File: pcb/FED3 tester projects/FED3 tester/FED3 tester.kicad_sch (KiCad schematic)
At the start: 27 parts, among them J1 USB4105-GF-A, U1 FT232RL, U2 LP5907MFX-3.3, U3 TPS79301-EP

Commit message: FED3 Tester - 1º routing finalizado
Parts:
- added L2: 40R@100MHz, Resistor_SMD:R_0805_2012Metric, symbol Device:R
- C1, C2, C3: footprint Capacitor_SMD:C_0402_1005Metric_Pad0.74x0.62mm_HandSolder -> Capacitor_SMD:C_0402_1005Metric
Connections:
- net USB+5V: now also L2.1
- new net RELAY+5V: L2.2
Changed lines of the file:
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@@
 	)
 	(junction
+		(at 81.28 36.83)
+		(diameter 0)
+		(color 0 0 0 0)
+	)
+	(junction
 		(at 147.32 88.9)
 		(diameter 0)
@@
 	(wire
 		(pts
+			(xy 81.28 36.83) (xy 85.09 36.83)
+		)
+		(stroke
+			(width 0)
+			(type default)
+		)
+	)
+	(wire
+		(pts
 			(xy 92.71 162.56) (xy 92.71 165.1)
 		)
@@
 	(wire
 		(pts
+			(xy 97.79 27.94) (xy 97.79 36.83)
+		)
+		(stroke
+			(width 0)
+			(type default)
+		)
+	)
+	(wire
+		(pts
 			(xy 74.93 41.91) (xy 71.12 41.91)
 		)
@@
 	(wire
 		(pts
+			(xy 92.71 36.83) (xy 97.79 36.83)
+		)
+		(stroke
+			(width 0)
+			(type default)
+		)
+	)
+	(wire
+		(pts
 			(xy 92.71 153.67) (xy 87.63 153.67)
 		)
@@
 	)
 	(symbol
+		(lib_id "power:+5V")
+		(at 97.79 27.94 0)
+		(mirror y)
+		(unit 1)
+		(exclude_from_sim no)
+		(in_bom yes)
+		(on_board yes)
+		(dnp no)
+		(property "Reference" "#PWR094"
+			(at 97.79 31.75 0)
+			(effects
+				(font
+					(size 1.27 1.27)
+				)
+				(hide yes)
+			)
+		)
+		(property "Value" "RELAY+5V"
+			(at 97.409 23.5458 0)
+			(effects
+				(font
+					(size 1.27 1.27)
+				)
+			)
+		)
+		(property "Footprint" ""
+			(at 97.79 27.94 0)
+			(effects
+				(font
+					(size 1.27 1.27)
+				)
+				(hide yes)
+			)
+		)
+		(property "Datasheet" ""
+			(at 97.79 27.94 0)
+			(effects
+				(font
+					(size 1.27 1.27)
+				)
+				(hide yes)
+			)
+		)
+		(property "Description" "Power symbol creates a global label with name \"+5V\""
+			(at 97.79 27.94 0)
+			(effects
+				(font
+					(size 1.27 1.27)
+				)
+				(hide yes)
+			)
+		)
+		(pin "1"
+		)
+		(instances
+			(project "FED3 tester"
+				(path "/2ba63f12-2fcd-4471-9636-2762cde37de8"
+					(reference "#PWR094")
+					(unit 1)
+				)
+			)
+		)
+	)
+	(symbol
 		(lib_id "power:GNDD")
 		(at 111.76 44.45 0)
@@
 			)
 		)
-		(property "Footprint" "Capacitor_SMD:C_0402_1005Metric_Pad0.74x0.62mm_HandSolder"
+		(property "Footprint" "Capacitor_SMD:C_0402_1005Metric"
 			(at 138.43 31.75 0)
 			(effects
@@
 	)
 	(symbol
+		(lib_id "Device:R")
+		(at 88.9 36.83 90)
+		(mirror x)
+		(unit 1)
+		(exclude_from_sim no)
+		(in_bom yes)
+		(on_board yes)
+		(dnp no)
+		(property "Reference" "L2"
+			(at 88.9 31.5722 90)
+			(effects
+				(font
+					(size 1.27 1.27)
+				)
+			)
+		)
+		(property "Value" "40R@100MHz"
+			(at 88.9 33.8836 90)
+			(effects
+				(font
+					(size 1.27 1.27)
+				)
+			)
+		)
+		(property "Footprint" "Resistor_SMD:R_0805_2012Metric"
+			(at 88.9 35.052 90)
+			(effects
+				(font
+					(size 1.27 1.27)
+				)
+				(hide yes)
+			)
+		)
+		(property "Datasheet" "~"
+			(at 88.9 36.83 0)
+			(effects
+				(font
+					(size 1.27 1.27)
+				)
+				(hide yes)
+			)
+		)
+		(property "Description" "FERRITE BEAD SMD 40Ω 2A 50mΩ"
+			(at 88.9 36.83 0)
+			(effects
+				(font
+					(size 1.27 1.27)
+				)
+				(hide yes)
+			)
+		)
+		(property "MPN" "MI0805K400R-10"
+			(at 88.9 36.83 0)
+			(effects
+				(font
+					(size 1.27 1.27)
+				)
+				(hide yes)
+			)
+		)
+		(property "OEPSPN" "OEPS040003"
+			(at 88.9 36.83 0)
+			(effects
+				(font
+					(size 1.27 1.27)
+				)
+				(hide yes)
+			)
+		)
+		(pin "1"
+		)
+		(pin "2"
+		)
+		(instances
+			(project "FED3 tester"
+				(path "/2ba63f12-2fcd-4471-9636-2762cde37de8"
+					(reference "L2")
+					(unit 1)
+				)
+			)
+		)
+	)
+	(symbol
 		(lib_id "Device:C_Small")
 		(at 152.4 33.02 0)
@@
 			)
 		)
-		(property "Footprint" "Capacitor_SMD:C_0402_1005Metric_Pad0.74x0.62mm_HandSolder"
+		(property "Footprint" "Capacitor_SMD:C_0402_1005Metric"
 			(at 152.4 33.02 0)
 			(effects
@@
 			)
 		)
-		(property "Footprint" "Capacitor_SMD:C_0402_1005Metric_Pad0.74x0.62mm_HandSolder"
+		(property "Footprint" "Capacitor_SMD:C_0402_1005Metric"
 			(at 111.76 40.64 0)
 			(effects
@@
 			(project "FED3 tester"
 				(path "/2ba63f12-2fcd-4471-9636-2762cde37de8"
-					(page "3")
+					(page "2")
 				)
 			)

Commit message: FED3-tester
- 'final' - antes de revisão com o Filipe
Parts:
- C1, C2, C3: MPN C1005X7R1E104K050BB -> CGA2B3X7R1H104K050BB; OEPSPN OEPS010050 -> OEPS010016; TYPE (none) -> SMD
- C10: value 15pF -> 150pF; MPN TBD -> C1608C0G1H150J080AA; OEPSPN TBD -> OEPS010072; TYPE (none) -> SMD
- C11, C12, C4, C5, C6, C7, C8, C9, J1, L1, L2, R1, R3, R4, R5, R6, U1, U2, U3: TYPE (none) -> SMD
- C13: MPN TBD -> GRM155R71E103KA01D; OEPSPN TBD -> OEPS010067; TYPE (none) -> SMD
- R2: MPN CRCW040210K0FKED -> CPF0402B10KE1; OEPSPN OEPS020030 -> OEPS020043; TYPE (none) -> SMD
- R7: value 60k8 -> 61k2; MPN ?? -> TBD; OEPSPN ?? -> TBD; TYPE (none) -> SMD
- R8: MPN ?? -> RC0603FR-0730K1L; OEPSPN ?? -> OEPS020132; TYPE (none) -> SMD
- TP1: MPN (none) -> n.a; OEPSPN (none) -> n.a; TYPE (none) -> n.a

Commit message: FED 3 tester - actualizados novos OEPSPN & MPN; ainda 1 em falta
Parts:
- R7: MPN TBD -> RN73R1ETTP6122B25; OEPSPN TBD -> OEPS020214
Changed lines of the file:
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@@
 			)
 		)
-		(property "MPN" "TBD"
+		(property "MPN" "RN73R1ETTP6122B25"
 			(at 78.867 163.068 0)
 			(effects
@@
 			)
 		)
-		(property "OEPSPN" "TBD"
+		(property "OEPSPN" "OEPS020214"
 			(at 87.63 160.02 0)
 			(effects

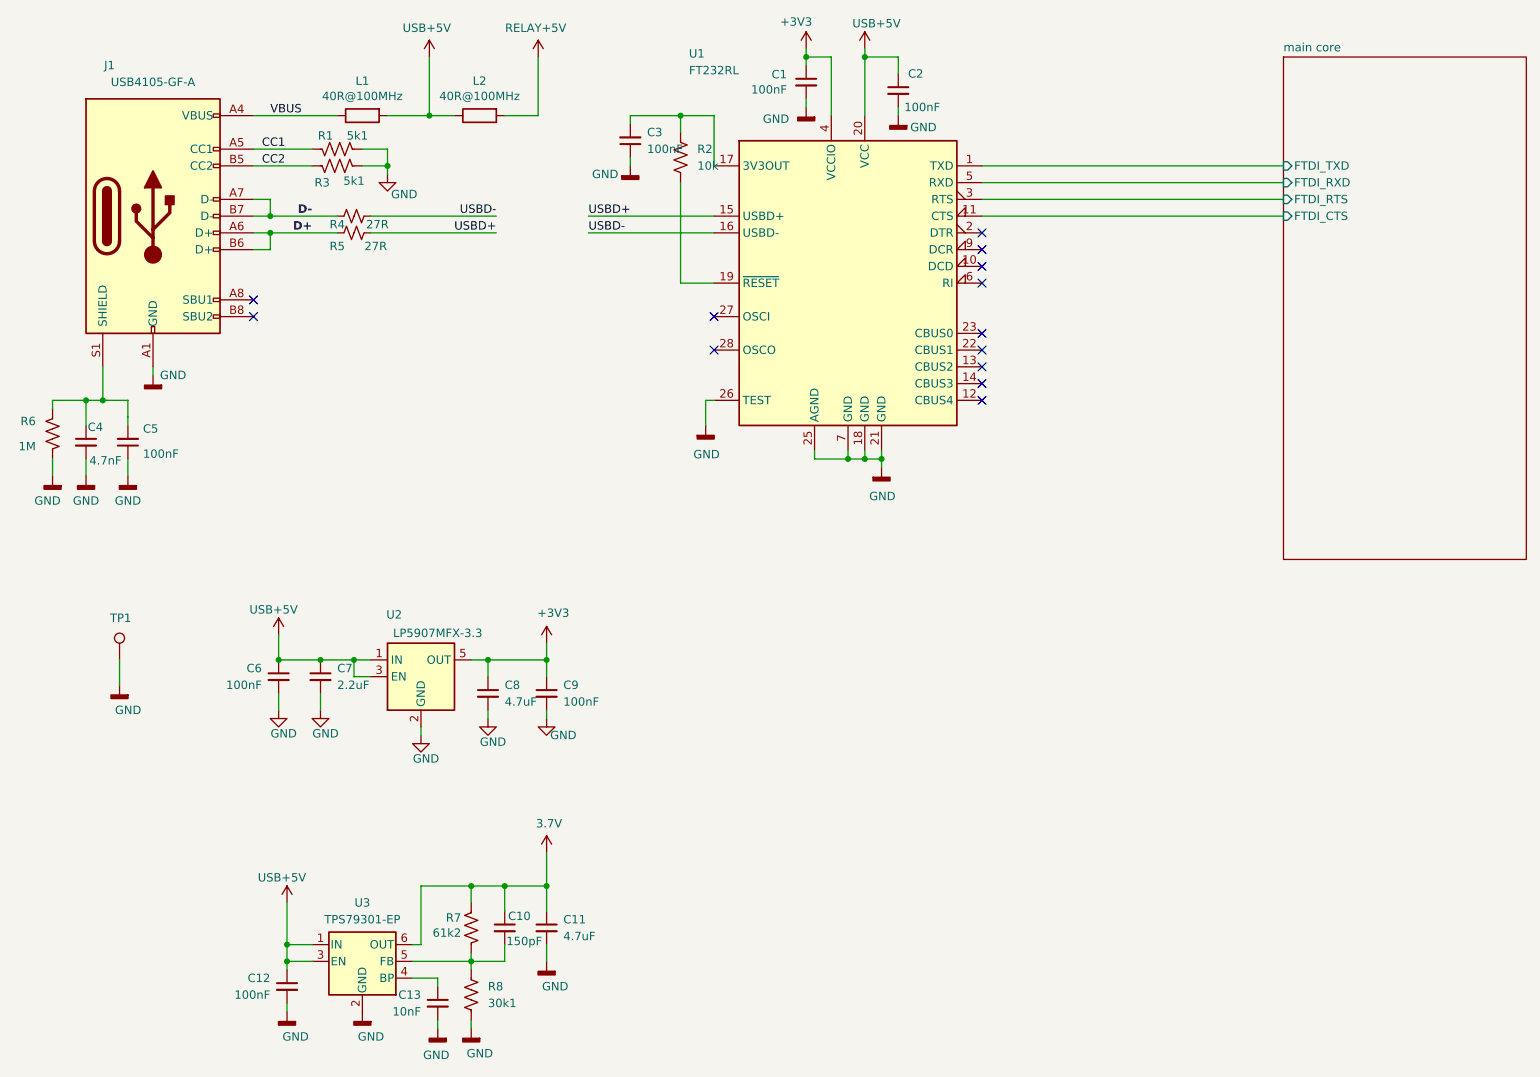
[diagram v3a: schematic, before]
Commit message: tunning com v.7.7
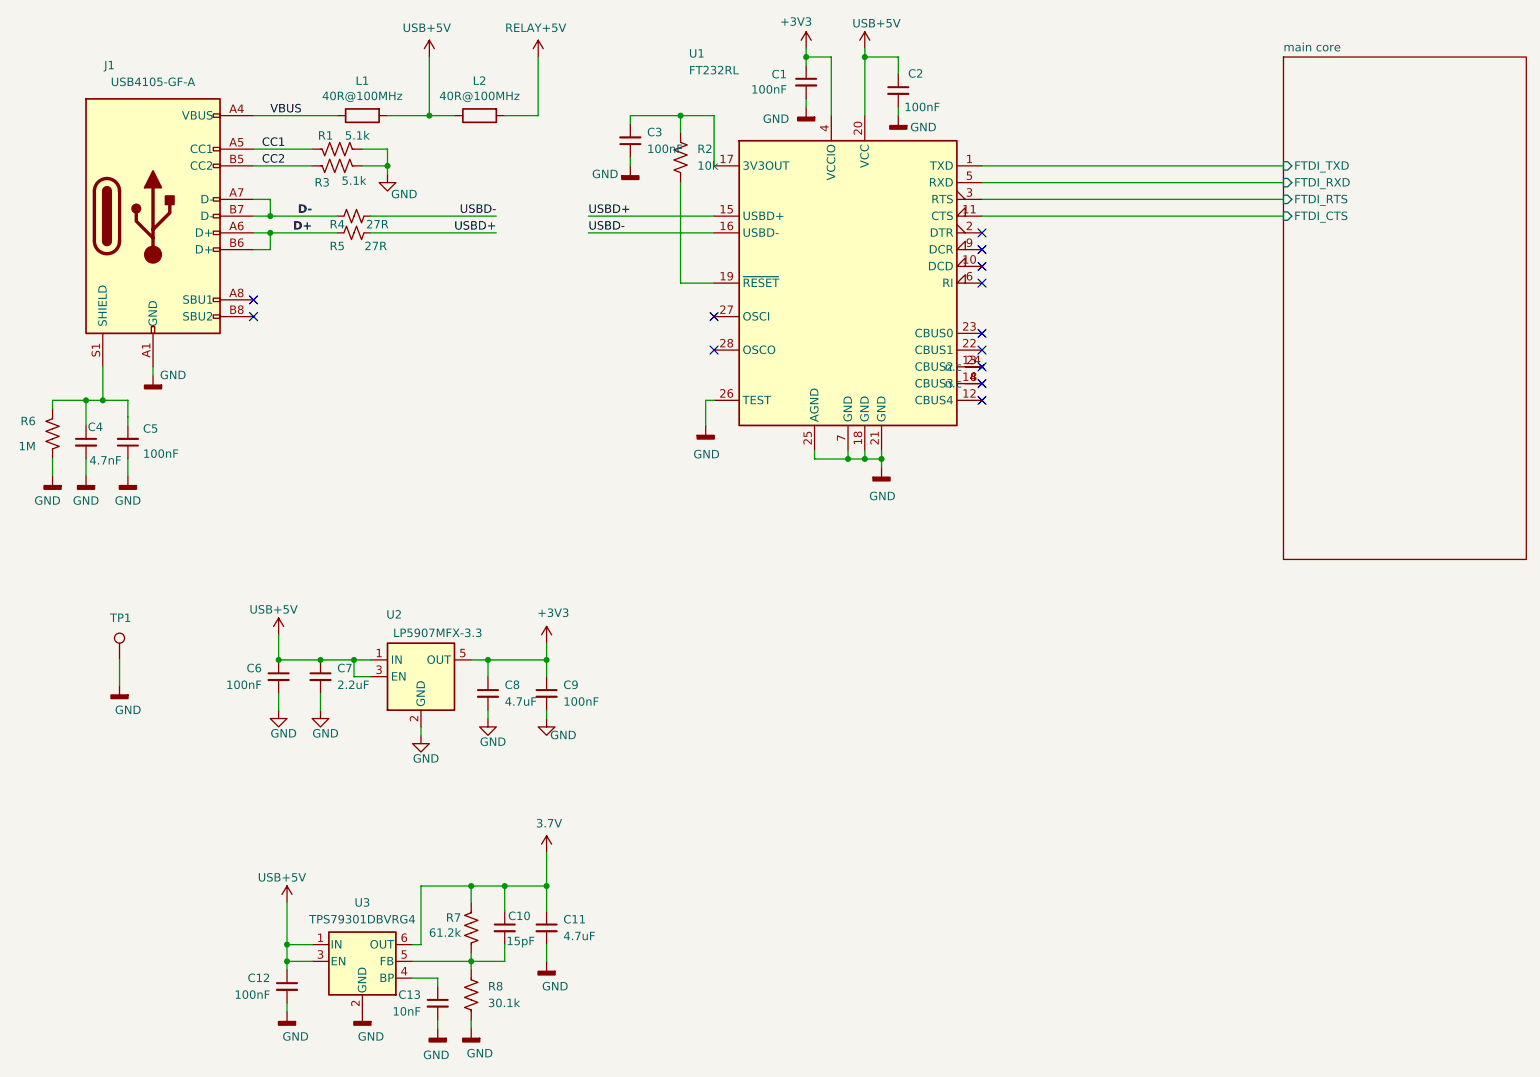
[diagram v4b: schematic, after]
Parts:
- C1, C12, C2, C3, C5, C6, C9: TYPE SMD -> (none); TempCo (none) -> X7R; Tolerance (none) -> 10%; Voltage (none) -> 50V
- C10: value 150pF -> 15pF; footprint Capacitor_SMD:C_0402_1005Metric -> Capacitor_SMD:C_0603_1608Metric; TYPE SMD -> (none); TempCo (none) -> C0G; Tolerance (none) -> 5%; Voltage (none) -> 50V
- C11, C8: TYPE SMD -> (none); TempCo (none) -> X6S; Tolerance (none) -> 10%; Voltage (none) -> 16V
- C13: TYPE SMD -> (none); TempCo (none) -> X7R; Tolerance (none) -> 10%; Voltage (none) -> 25V
- C4: TYPE SMD -> (none); TempCo (none) -> X7R; Tolerance (none) -> 10%; Voltage (none) -> 100V
- C7: TYPE SMD -> (none); TempCo (none) -> X5R; Tolerance (none) -> 10%; Voltage (none) -> 25V
- J1, L1, L2, U1, U2: TYPE SMD -> (none)
- R1, R3: value 5k1 -> 5.1k; TYPE SMD -> (none); Tolerance (none) -> 1%
- R2: TYPE SMD -> (none); Tolerance (none) -> 0.1%
- R4, R5, R6: TYPE SMD -> (none); Tolerance (none) -> 1%
- R7: value 61k2 -> 61.2k; TYPE SMD -> (none); Tolerance (none) -> 0.1%
- R8: value 30k1 -> 30.1k; footprint Resistor_SMD:R_0402_1005Metric -> Resistor_SMD:R_0603_1608Metric; TYPE SMD -> (none); Tolerance (none) -> 1%
- TP1: TYPE n.a -> (none)
- U3: value TPS79301-EP -> TPS79301DBVRG4; TYPE SMD -> (none)
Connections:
- net at U1.13 (CBUS2): now also U1.24 (n.c)
- net at U1.14 (CBUS3): now also U1.8 (n.c)
